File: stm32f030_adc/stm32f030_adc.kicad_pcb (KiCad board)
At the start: 2 copper layers, 46 parts, among them Q1 BC337, U1 STM32F103C6Tx, U2 AMS1117-3.3, X1 USB_B_Micro, Y2 8 MHz

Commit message: [schematics] Impl |  Finished placement on "Vert" version
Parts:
- moved R19 38.7 mm to (218.5, 69.8), turned to -90 degrees
- moved R14 35.4 mm to (187.0, 82.4), turned to -90 degrees
- moved R12 31.4 mm to (190.0, 82.4), turned to -90 degrees
- moved R8 29.2 mm to (227.0, 94.9), turned to -90 degrees
- moved R18 25.9 mm to (221.5, 69.8), turned to -90 degrees
- moved R15 25.4 mm to (224.0, 94.9), turned to -90 degrees
- moved MK1 22.5 mm to (187.5, 110.0)
- moved R22 21.7 mm to (221.0, 94.9), turned to -90 degrees
- moved R16 19.2 mm to (215.5, 69.8), turned to -90 degrees
- moved R11 18.6 mm to (193.0, 94.9), turned to -90 degrees
- moved R9 15.0 mm to (218.0, 105.1), turned to 90 degrees
- moved R6 12.2 mm to (227.6, 110.6), turned to 180 degrees
- moved C10 11.5 mm to (212.0, 68.5), turned to 180 degrees
- moved C6 11.5 mm to (212.0, 80.5), turned to 180 degrees
- moved C16 10.7 mm to (222.2, 87.5)
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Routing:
- net Net-(U2-ADJ): track 21.3 -> 0.00 mm
- net +3V3: track 12.0 -> 0.00 mm
- net /Power and MCU/USB_D+: track 11.4 -> 0.00 mm
- net 5V_USB: track 8.73 -> 0.00 mm
- net GNDREF: track 3.71 -> 0.00 mm

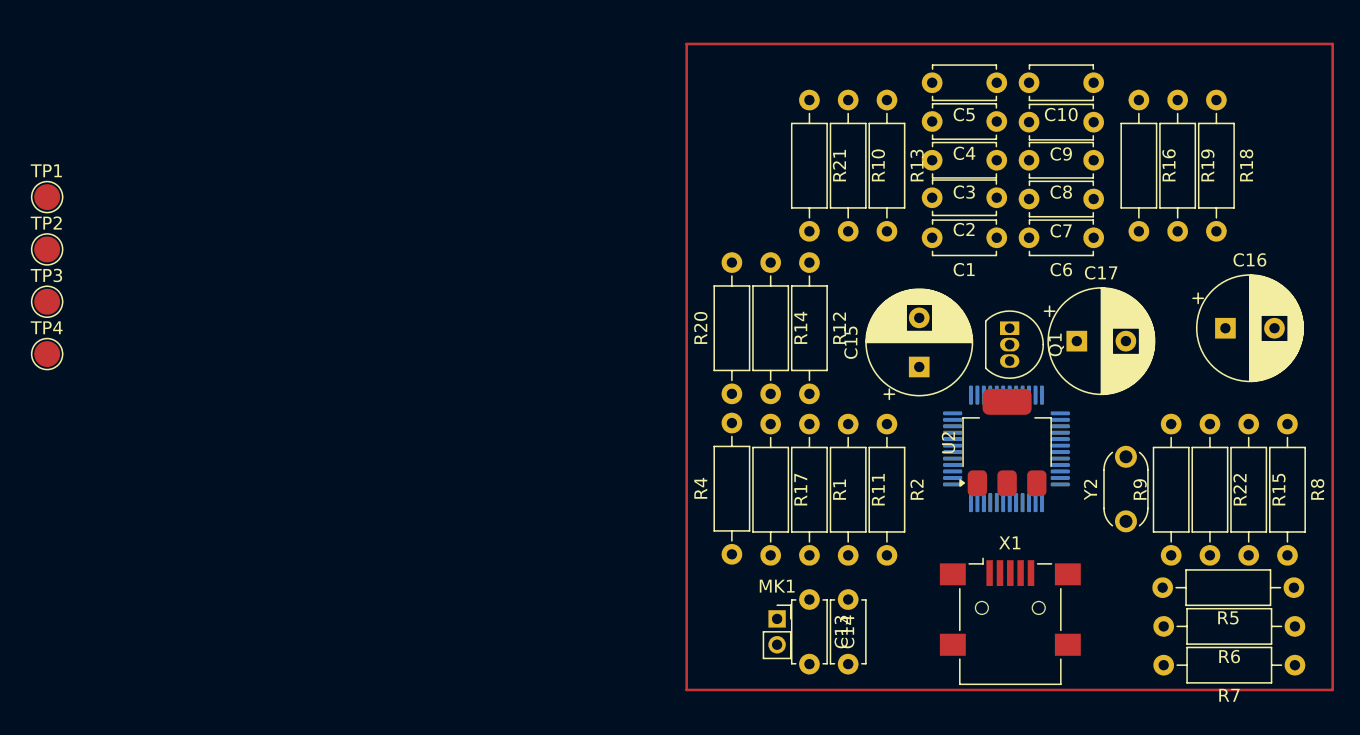
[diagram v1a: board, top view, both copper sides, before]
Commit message: [schematics] Impl |  Added DRC exclusions: unconnected grounds (it will be connected, because the USB shield is connected to the ground
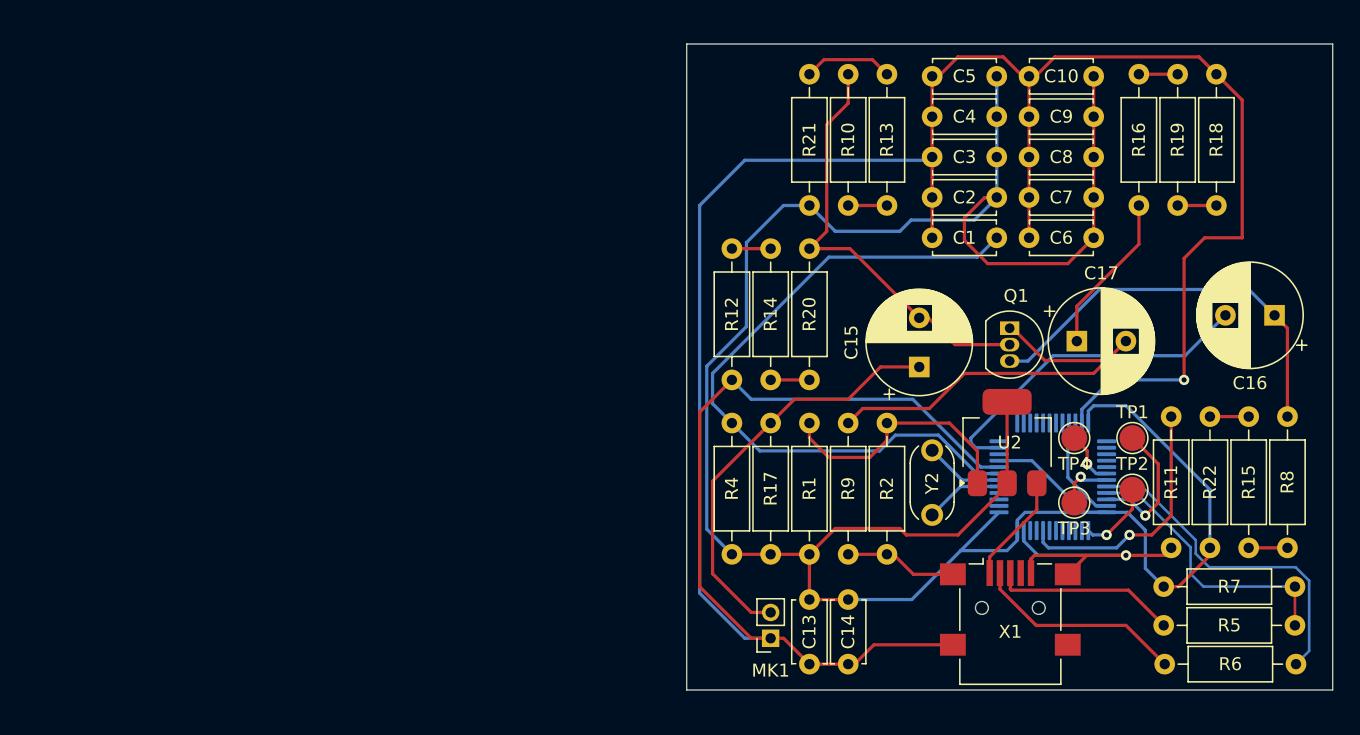
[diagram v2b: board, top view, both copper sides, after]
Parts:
- moved TP1 86.0 mm to (215.0, 96.0)
- moved TP2 86.0 mm to (215.0, 100.0)
- moved TP3 81.0 mm to (210.5, 101.0), turned to 180 degrees
- moved TP4 79.8 mm to (210.5, 96.0), turned to 180 degrees
- moved R11 26.8 mm to (218.0, 104.5), turned to 90 degrees
- moved R9 25.0 mm to (193.0, 105.0)
- moved Y2 15.0 mm to (199.5, 102.0)
- moved R12 10.9 mm to (184.0, 91.5), turned to 90 degrees
- moved R5 10.5 mm to (217.4, 110.5), turned to 0 degrees
- moved R6 10.5 mm to (217.5, 113.5), turned to 0 degrees
- moved R1 10.1 mm to (190.0, 105.0), turned to 90 degrees
- moved R15 9.58 mm to (224.0, 104.5), turned to 90 degrees
- moved R10 8.69 mm to (196.0, 78.0), turned to 90 degrees
- moved R19 8.16 mm to (218.5, 78.0), turned to 90 degrees
- moved R20 6.10 mm to (190.0, 91.5)
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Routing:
- net GNDREF: track 0.00 -> 247.3 mm, vias 0 -> 2
- net +3V3: track 0.00 -> 191.6 mm
- net Net-(U1-NRST): track 0.00 -> 54.1 mm
- net Net-(Q1-B): track 0.00 -> 33.3 mm
- net Net-(Q1-E): track 0.00 -> 32.7 mm
- net Net-(MK1-+): track 0.00 -> 32.6 mm
- net Net-(Q1-C): track 0.00 -> 31.9 mm
- net /Electret AMP/MIC_AMP_OUT: track 0.00 -> 26.3 mm
- net /Power and MCU/USB_D-: track 0.00 -> 26.2 mm
- net /Power and MCU/USB_D+: track 0.00 -> 21.8 mm
- net Net-(U2-ADJ): track 0.00 -> 20.1 mm
- net Net-(U1-BOOT0): track 0.00 -> 19.7 mm, vias 0 -> 1
- net Net-(X1-D-): track 0.00 -> 16.4 mm
- net Net-(X1-D+): track 0.00 -> 14.3 mm
- net Net-(C17-Pad1): track 0.00 -> 12.5 mm
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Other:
- board outline added: 50 x 50 mm
